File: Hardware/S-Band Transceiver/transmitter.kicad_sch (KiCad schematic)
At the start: 0 parts

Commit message: Updates to schematic
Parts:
- added C40, C41: 10nF, symbol Device:C_Small
- added L5: 100nF, symbol Device:L_Small
- added R14: 3900, symbol Device:R_Small_US
- added R15: 1, symbol Device:R_Small_US
- added U13: GALI-39, Package_TO_SOT_SMD:SOT-89-3, symbol RF_Amplifier:GALI-39
- added U14: LT3092xST, Package_TO_SOT_SMD:SOT-223-3_TabPin2, symbol Reference_Current:LT3092xST
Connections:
- new net: C40.1, L5.2, U13.3
- new net: R14.1, U14.1
- new net: L5.1, R14.2, R15.2
- new net: R15.1, U14.2
- new net: C41.2, U13.1
- new net +5V: U14.3
- new net GND: U13.2 (GND)
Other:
- note added: "35mA"
- note added: "DAT-31A-PP+ 31dB 5-bit digital atten. Parallel control interface https://www.minicircuits.com/pdfs/DAT-31A-PP+.pdf"
- note added: "PE44820 8-bit phase shifter 1.7-2.2 GHz SPI https://www.psemi.com/pdf/datasheets/pe44820ds.pdf"

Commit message: Updates to schematic
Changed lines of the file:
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@@
 	(text "PE44820\n8-bit phase shifter\n1.7-2.2 GHz\nSPI\nhttps://www.psemi.com/pdf/datasheets/pe44820ds.pdf"
 		(exclude_from_sim no)
-		(at 75.184 50.546 0)
+		(at 71.628 49.784 0)
 		(effects
 			(font

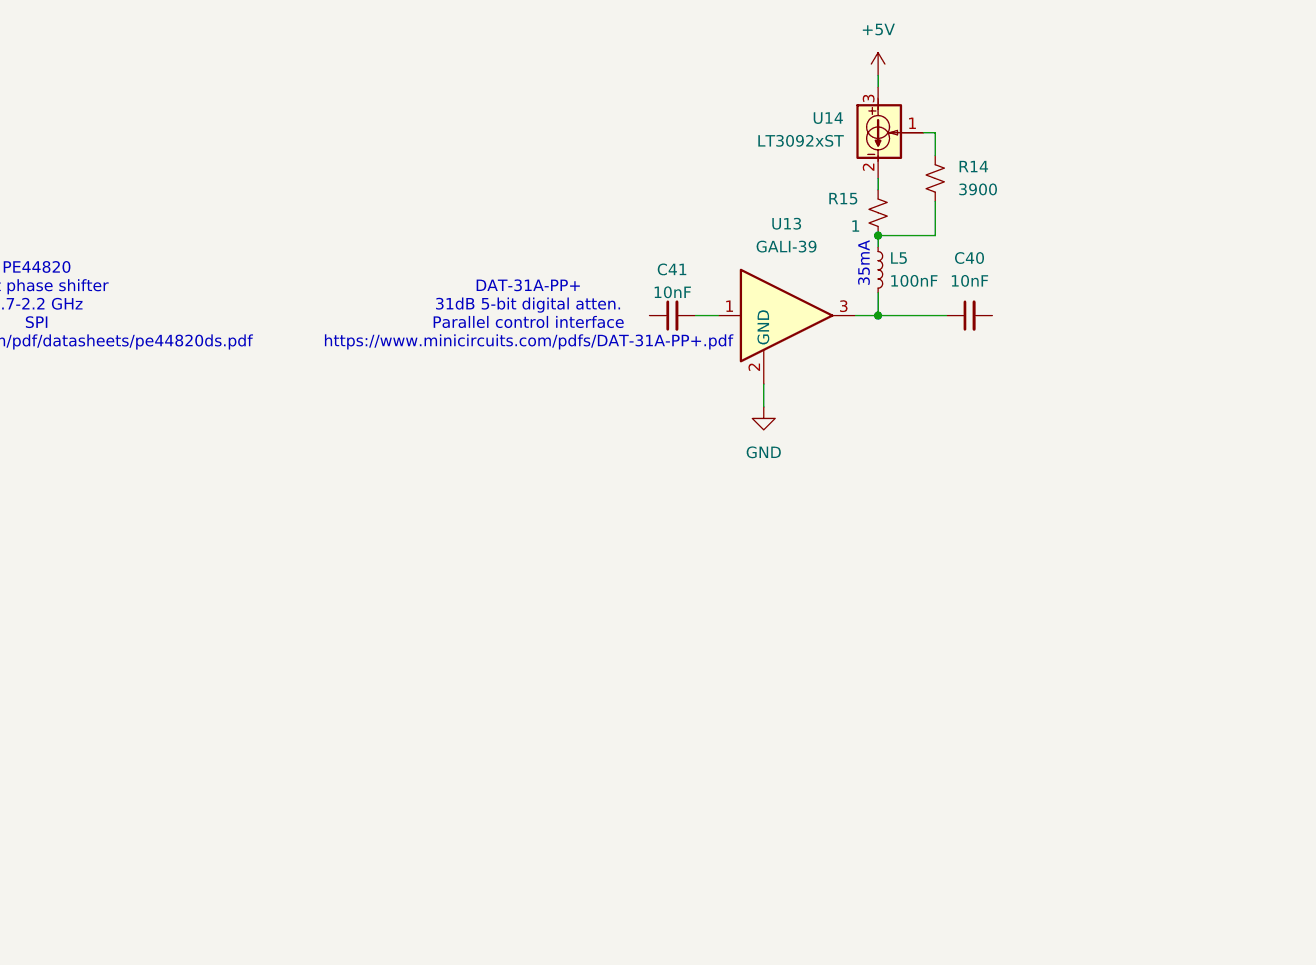
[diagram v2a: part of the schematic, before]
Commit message: Updates to power supply schematic
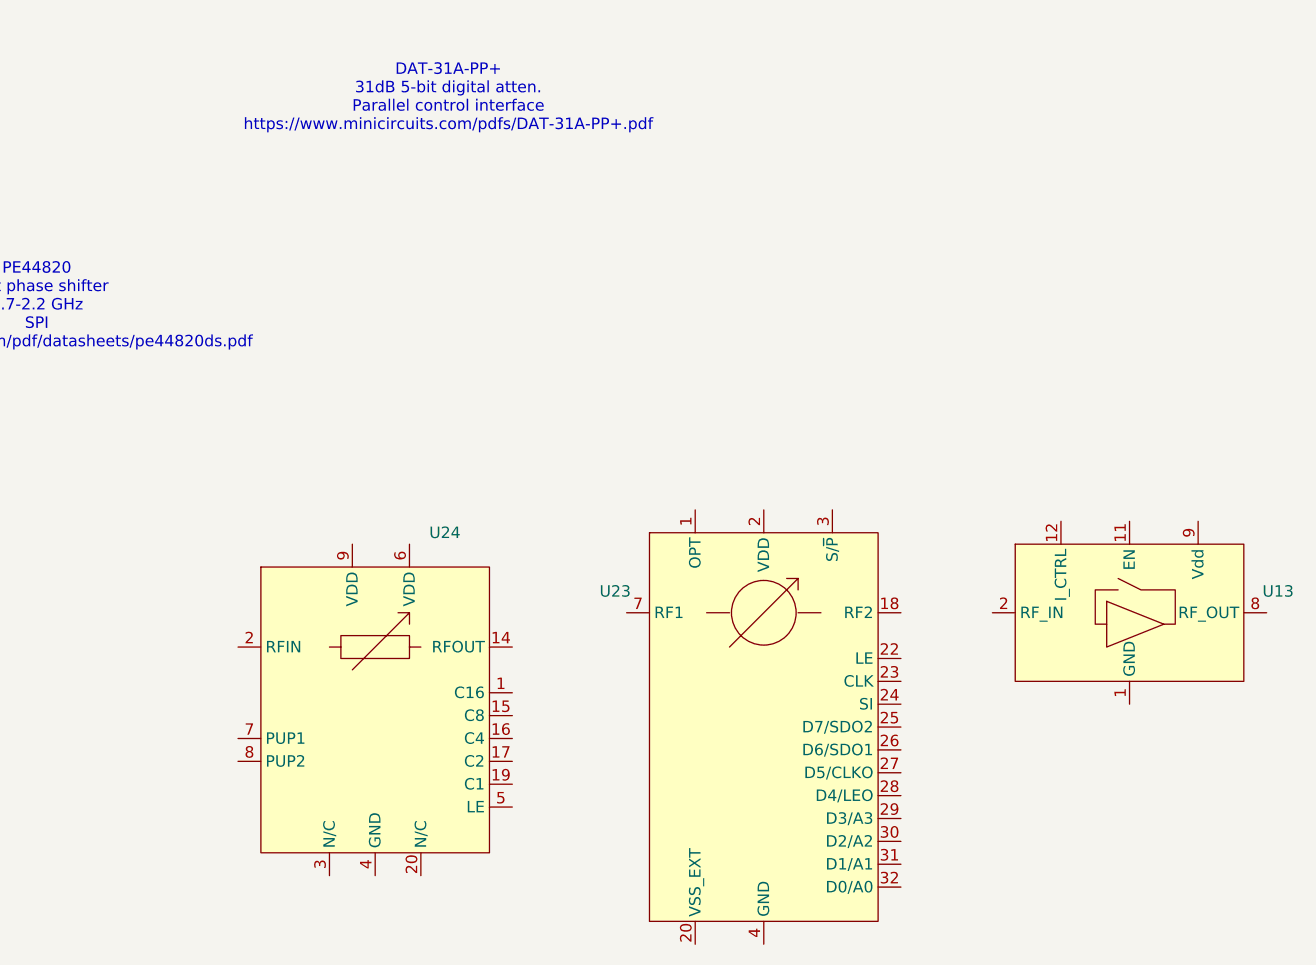
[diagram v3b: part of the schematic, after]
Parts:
- removed C40, C41: 10nF, symbol Device:C_Small
- removed L5: 100nF, symbol Device:L_Small
- removed R14: 3900, symbol Device:R_Small_US
- removed R15: 1, symbol Device:R_Small_US
- removed U13: GALI-39, Package_TO_SOT_SMD:SOT-89-3, symbol RF_Amplifier:GALI-39
- removed U14: LT3092xST, Package_TO_SOT_SMD:SOT-223-3_TabPin2, symbol Reference_Current:LT3092xST
- added U13: ~, _tim-RF-Mini-Circuits:DQ1225, symbol _tim-RF:TSS-53LNB3+
- added U23: ~, Package_DFN_QFN:QFN-32-1EP_5x5mm_P0.5mm_EP3.6x3.6mm, symbol _tim-RF:PE44820
- added U24: ~, Package_DFN_QFN:QFN-20-1EP_4x4mm_P0.5mm_EP2.5x2.5mm, symbol _tim-RF:DAT-31A+
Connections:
- net GND: now also U23.10 (GND), U23.11 (GND), U23.12 (GND), U23.13 (GND), U23.14 (GND), U23.15 (GND), U23.16 (GND), U23.17 (GND), U23.19 (GND), U23.21 (GND), U23.33 (PAD), U23.4 (GND), U23.5 (GND), U23.6 (GND), U23.8 (GND), U23.9 (GND), U24.10 (GND), U24.11 (GND), U24.12 (GND), U24.13 (GND), U24.18 (GND), U24.21 (GND), U24.4 (GND)
- new net: U13.1 (GND), U13.10 (GND), U13.13 (GND), U13.3 (GND), U13.4 (GND), U13.5 (GND), U13.6 (GND), U13.7 (GND)
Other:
- note removed: "35mA"

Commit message: Updating schematic
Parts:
- added C68, C69, C70, C71, C74, C76, C82, C85: 100pF, symbol Device:C_Small
- added C72, C73, C75, C77, C81, C83, C84: 100nF, symbol Device:C_Small
- added C78: 10pF, symbol Device:C_Small
- added C79, C80: 10nF, symbol Device:C_Small
- added J7: SMA, symbol Connector:Conn_Coaxial
- added L3: 100nH, symbol Device:L_Small
- added R29: 50, symbol Device:R_Small_US
- added R30: 3.92k, symbol Device:R_Small_US
- added R31, R32, R33, R34, R35, R36, R37: 10k, symbol Device:R_Small_US
- added R38: 60.4, symbol Device:R_Small_US
- added R39: 3.74, symbol Device:R_Small_US
- added R40: 1.5k, symbol Device:R_Small_US
- added R41: 270, symbol Device:R_Small_US
- added R42: 2k, symbol Device:R_Small_US
- added U19: DCW-22-332+, _tim-RF-Mini-Circuits:JC0603C, symbol _tim-RF:DCW-22-332+
- added U25: ADL5906, Package_DFN_QFN:QFN-16-1EP_4x4mm_P0.65mm_EP2.1x2.1mm_ThermalVias, symbol _tim-RF:ADL5906
- U13: value ~ -> TSS-53LNB3+
- U23: value ~ -> PE44820
- U24: value ~ -> DAT-31A+
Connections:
- net GND: now also U13.1 (GND), U13.10 (GND), U13.13 (GND), U13.3 (GND), U13.4 (GND), U13.5 (GND), U13.6 (GND), U13.7 (GND), U23.20 (VSS_EXT), C71.1, C72.1, C73.2, C74.2, C75.1, C76.1, C77.2, C78.2, C79.2, C81.1, C82.1, C83.2, C84.2, C85.2, J7.2 (Ext), R29.1, R31.1, R32.1, R33.1, R37.1, R38.2, R41.1, R42.2, U19.2 (GND), U19.5 (GND), U25.17 (GND), U25.4 (GND), U25.9 (GND)
- net at U23.1 (OPT): now also R37.2
- net at U23.18 (RF2): now also C69.1
- net +3.3VA: now reaches U23.2 (VDD)
- net +3.3VA: now also U24.6 (VDD), U24.9 (VDD), C71.2, C72.2, C73.1, C74.1, C75.2, C76.2, C77.1, C78.1, L3.1, R34.2, R35.2, R36.1
- net TX_PHASE_LE: now reaches U23.22 (LE)
- net SCLK: now reaches U23.23 (CLK)
- net MOSI: now reaches U23.24 (SI)
- net MISO: now reaches U23.26 (D6/SDO1)
- net at U23.3 (S/~{P}): now also R36.2
- net at U23.7 (RF1): now also C68.2
- net TX_AMP_EN: now reaches U13.11 (EN)
- net TX_AMP_EN: now also R30.2
- net at U13.12 (I_CTRL): now also R30.1
- net at U13.2 (RF_IN): now also C69.2
- net at U13.8 (RF_OUT): now also U19.1 (IN)
- net at U13.9 (Vdd): now also L3.2
- net C16: now reaches U24.1 (C16)
- net at U24.14 (RFOUT): now also C68.1
- net C8: now reaches U24.15 (C8)
- net C4: now reaches U24.16 (C4)
- net C2: now reaches U24.17 (C2)
- net C1: now reaches U24.19 (C1)
- net SYNTH_TX: now reaches U24.2 (RFIN)
- net at U24.20 (N/C): now also R33.2
- net at U24.3 (N/C): now also R32.2
- net TX_ATTEN_LE: now reaches U24.5 (LE)
- net TX_ATTEN_LE: now also R31.2
- net at U24.7 (PUP1): now also R34.1
- net at U24.8 (PUP2): now also R35.1
- new net: R40.1, R41.2, U25.1 (TADJ)
- new net: R39.1, R40.2, U25.11 (VREF)
- new net: R39.2, R42.1, U25.12 (VTGT)
- new net: U25.13 (NIC), U25.16 (NIC), U25.2 (NIC)
- new net: C80.2, U25.14 (RFIN+)
- new net: C79.1, U25.15 (RFIN-)
- new net: C83.1, U25.5 (CRMS)
- new net: R29.2, U19.4 (TERM)
- new net: C70.1, U19.6 (OUT)
- new net +5V: C81.2, C82.2, C84.1, C85.1, U25.10 (VPOS2), U25.3 (VPOS1)
- new net RX_VRMS: U25.6 (VRMS), U25.7 (VSET)
- new net TX: C70.2, J7.1 (In)
- new net TX_MON: C80.1, R38.1, U19.3 (CPL)
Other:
- note added: "31.5dB startup: PUP1 HIGH PUP2 HIGH LE LOW"
- note added: "DC BLOCKING REQUIRED"
- note added: "VSS_EXT to GND: enable internal negative voltage generator"
- moved on the sheet: U13, U23, U24

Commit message: Updates to schematic
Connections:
- net RX_VRMS renamed TX_VRMS
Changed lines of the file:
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@@
 		)
 	)
-	(global_label "RX_VRMS"
+	(global_label "TX_VRMS"
 		(shape input)
 		(at 247.65 118.11 0)
@@
 		)
 		(property "Intersheetrefs" "${INTERSHEET_REFS}"
-			(at 259.1018 118.11 0)
+			(at 258.7994 118.11 0)
 			(effects
 				(font

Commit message: Updates to schematic
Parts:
- added U3: SN74LVC1G125DCK, Package_TO_SOT_SMD:SOT-23-5, symbol 74xGxx:SN74LVC1G125DCK
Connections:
- net +3.3VA: now also U3.5 (VCC)
- net GND: now also U3.3 (GND)
- net TX_AMP_EN: now also U3.2; no longer R30.2, U13.11 (EN)
- net MISO: no longer names the net of U23.26 (D6/SDO1)
- new net: R30.2, U13.11 (EN), U3.4
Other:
- note added: "0.5 to 5 GHz"
- note added: "1.7 to 2.2 GHz Extended Operation: 1.1-3.0 GHz"
- note added: "10 MHz to 10 GHz"
- note added: "1200 to 3300 MHz"
- note added: "DC to 4GHz"
- note added: "For direct parallel programming LE should be pulled high"
- note added: "PIN 20 Should always be low"

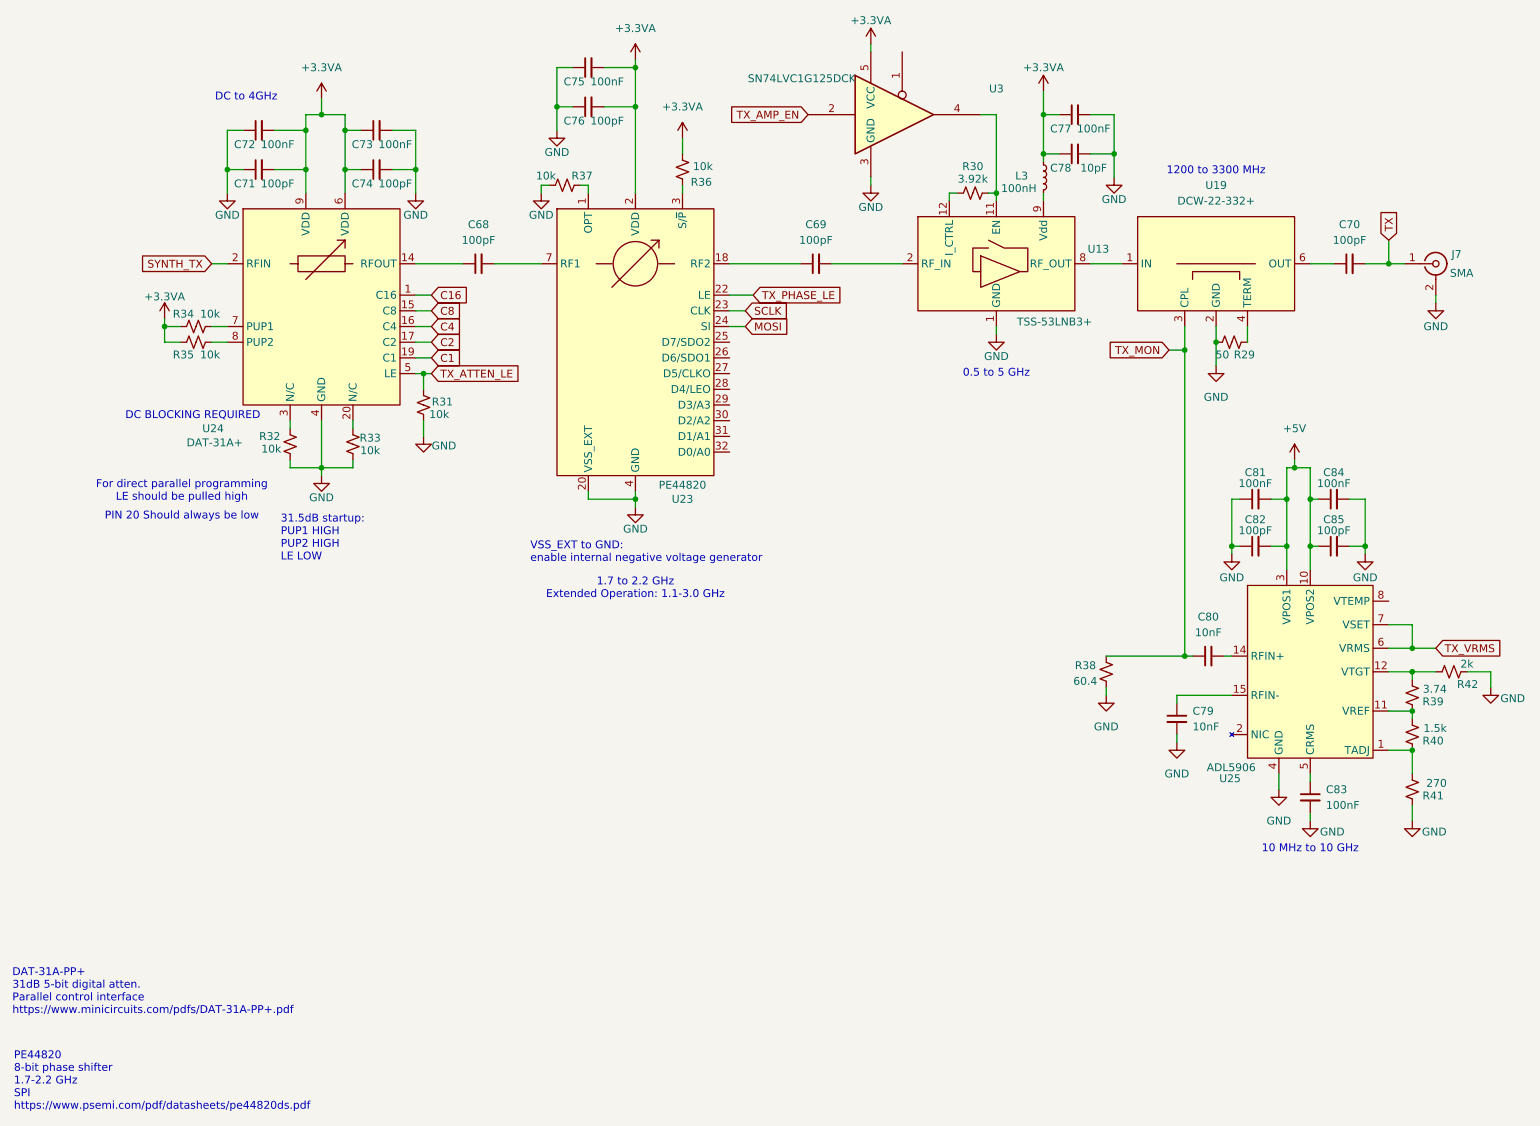
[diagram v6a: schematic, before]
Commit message: Updates to Schematic
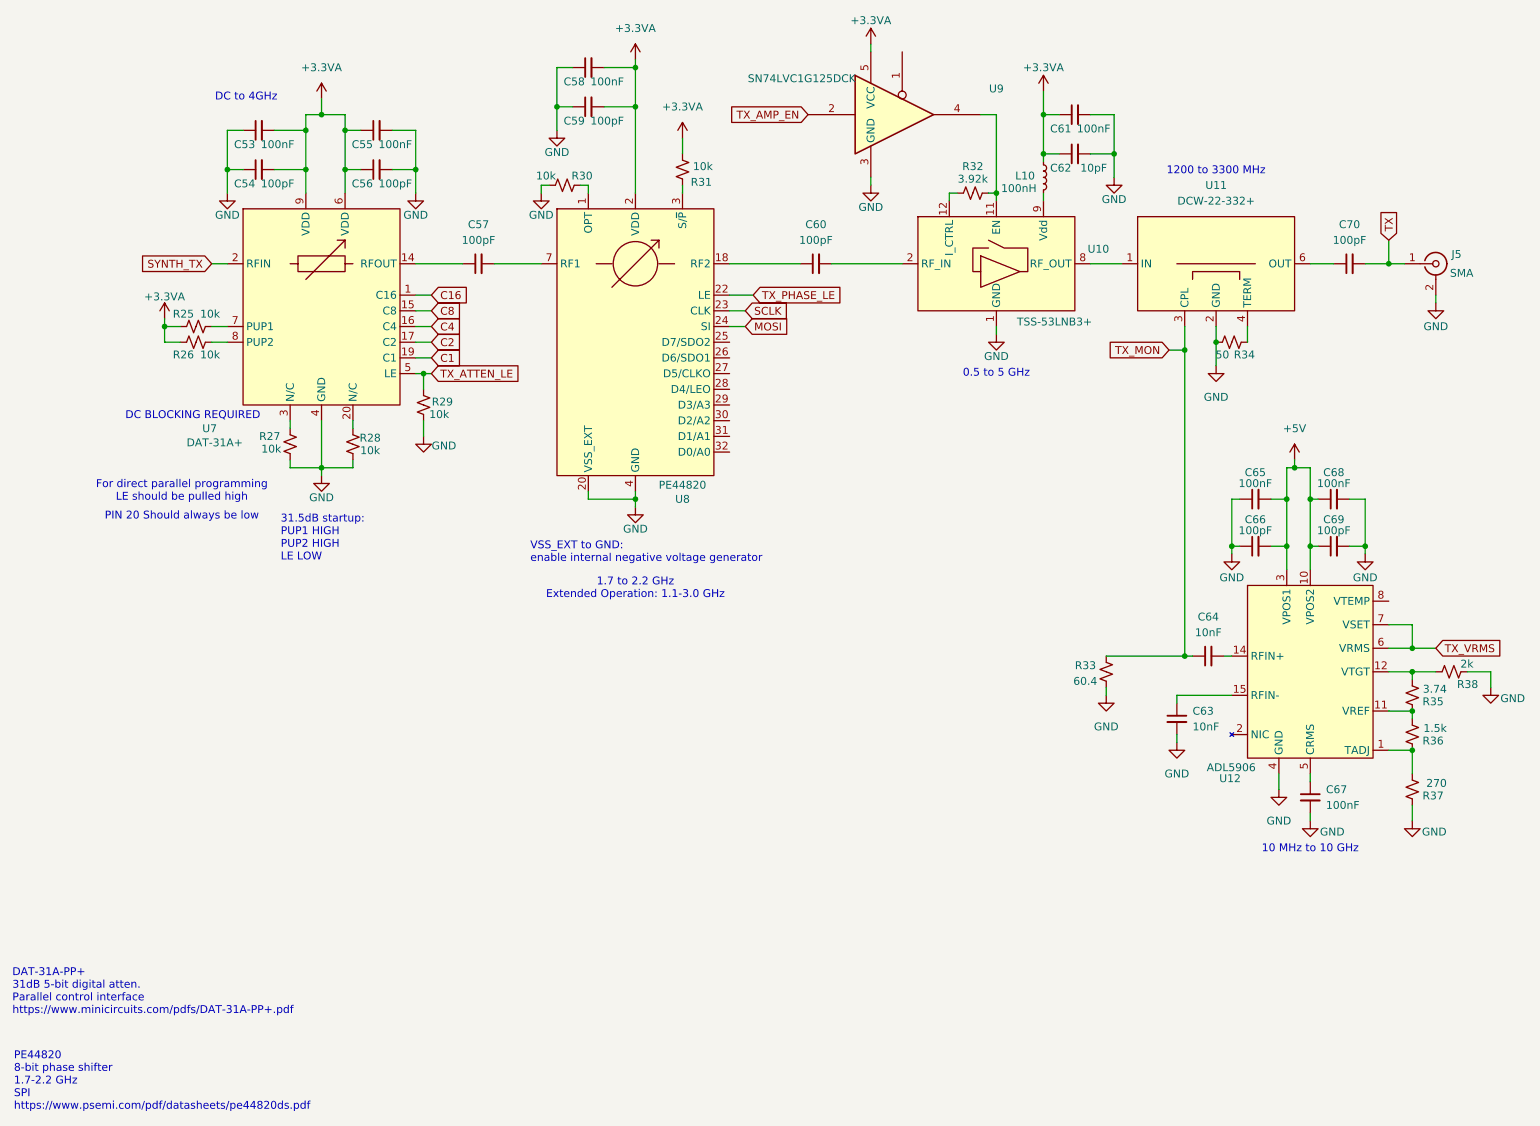
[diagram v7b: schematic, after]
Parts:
- renumbered C72 to C53, C71 to C54, C73 to C55, C74 to C56, C68 to C57, C75 to C58, C76 to C59, C69 to C60, C77 to C61, C78 to C62, C79 to C63, C80 to C64, C81 to C65, C82 to C66, C83 to C67, C84 to C68, C85 to C69, J7 to J5, L3 to L10, R34 to R25, R35 to R26, R32 to R27, R33 to R28, R31 to R29, R37 to R30, R36 to R31, R30 to R32, R38 to R33, R29 to R34, R39 to R35, R40 to R36, R41 to R37, R42 to R38, U13 to U10, U19 to U11, U25 to U12, U24 to U7, U23 to U8, U3 to U9
